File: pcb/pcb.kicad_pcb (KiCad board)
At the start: 2 copper layers, 27 parts, among them J1 Screw_Terminal_01x02, J2 Screw_Terminal_01x04, J3 Screw_Terminal_01x04, J4 Screw_Terminal_01x03, J5 Screw_Terminal_01x06, Q1 2N7000, Q2 2N7000, Q3 2N7000

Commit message: fix power line
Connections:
- A1 pad 1: Net-(A1-VMOT) -> Net-(D1-A)
- A1 pad 7: Net-(D1-K) -> Net-(D1-A)
- A2 pad 1: Net-(A1-VMOT) -> Net-(D1-A)
- A2 pad 7: unconnected-(A2-GND-Pad7) -> Net-(D1-A)
- A2 pad 8: unconnected-(A2-VMOT-Pad8) -> Net-(A1-VMOT)
- D1 pad 1: Net-(D1-K) -> Net-(A1-VMOT)
- D1 pad 2: Net-(A1-VMOT) -> Net-(D1-A)
- ESP32-S3 pad 22: Net-(A1-VMOT) -> Net-(D1-A)
- InputCap1 pad 1: Net-(A1-VMOT) -> Net-(D1-A)
- InputCap2 pad 1: Net-(A1-VMOT) -> Net-(D1-A)
- InputCap2 pad 2: Net-(D1-K) -> Net-(A1-VMOT)
- J1 pad 1: Net-(A1-VMOT) -> Net-(D1-A)
- J1 pad 2: Net-(D1-K) -> Net-(A1-VMOT)
- MovingBumperStart1 pad 1: Net-(A1-VMOT) -> Net-(D1-A)
- MovingBumper_back1 pad 1: Net-(A1-VMOT) -> Net-(D1-A)
- MovingBumper_front1 pad 1: Net-(A1-VMOT) -> Net-(D1-A)
- OutputCap1 pad 1: Net-(A1-VMOT) -> Net-(D1-A)
- OutputCap2 pad 1: Net-(A1-VMOT) -> Net-(D1-A)
- PTCFuse1 pad 1: Net-(D1-K) -> Net-(A1-VMOT)
- Q1 pad 1: Net-(A1-VMOT) -> Net-(D1-A)
- Q2 pad 1: Net-(A1-VMOT) -> Net-(D1-A)
- Q3 pad 1: Net-(A1-VMOT) -> Net-(D1-A)
- R1 pad 2: Net-(A1-VMOT) -> Net-(D1-A)
- Regulator1 pad 1: Net-(A1-VMOT) -> Net-(D1-A)
- Rehydration_bumper1 pad 1: Net-(A1-VMOT) -> Net-(D1-A)

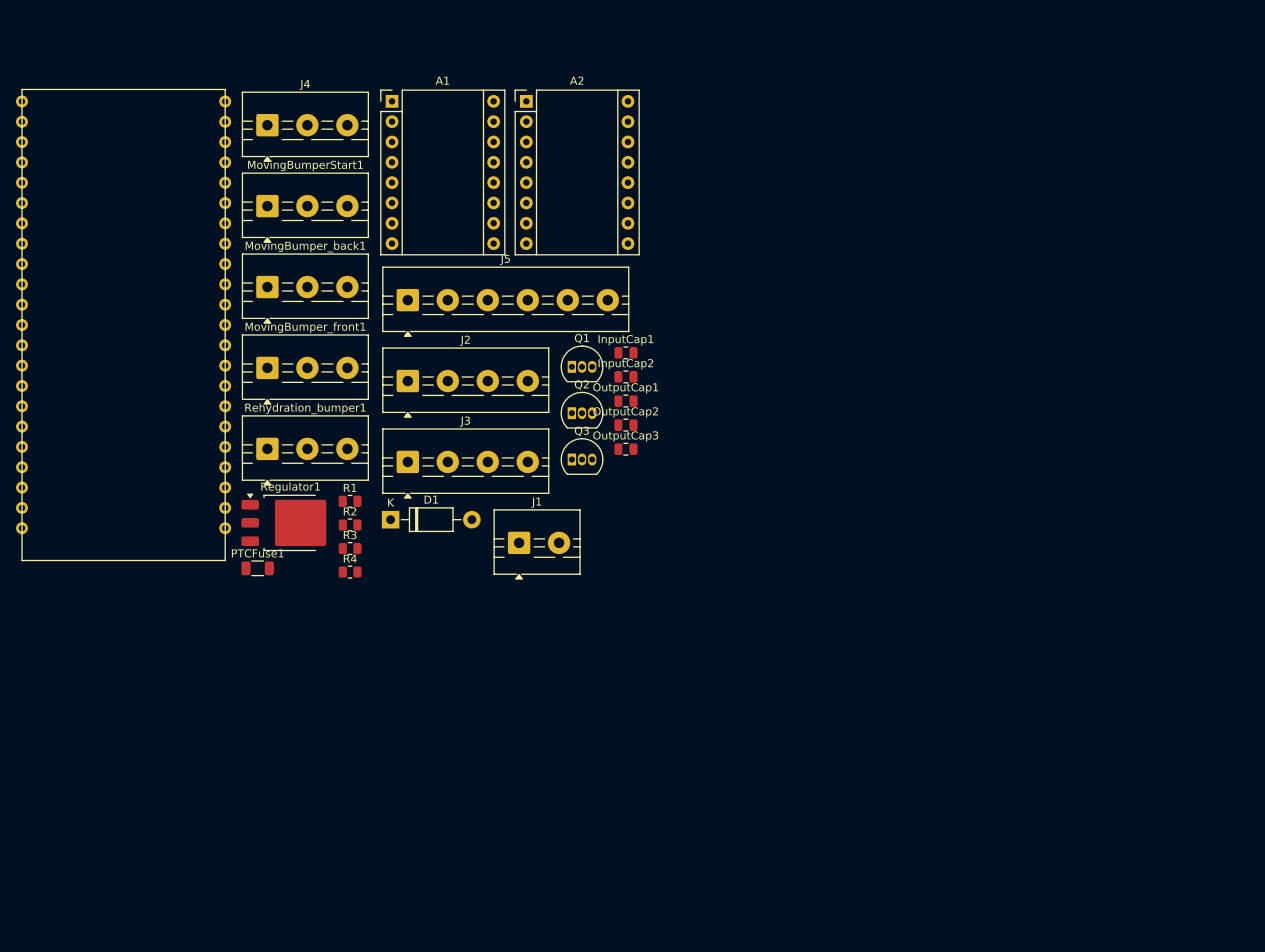
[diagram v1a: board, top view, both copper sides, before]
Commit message: auto-routed pcb, might make smaller or a better layout
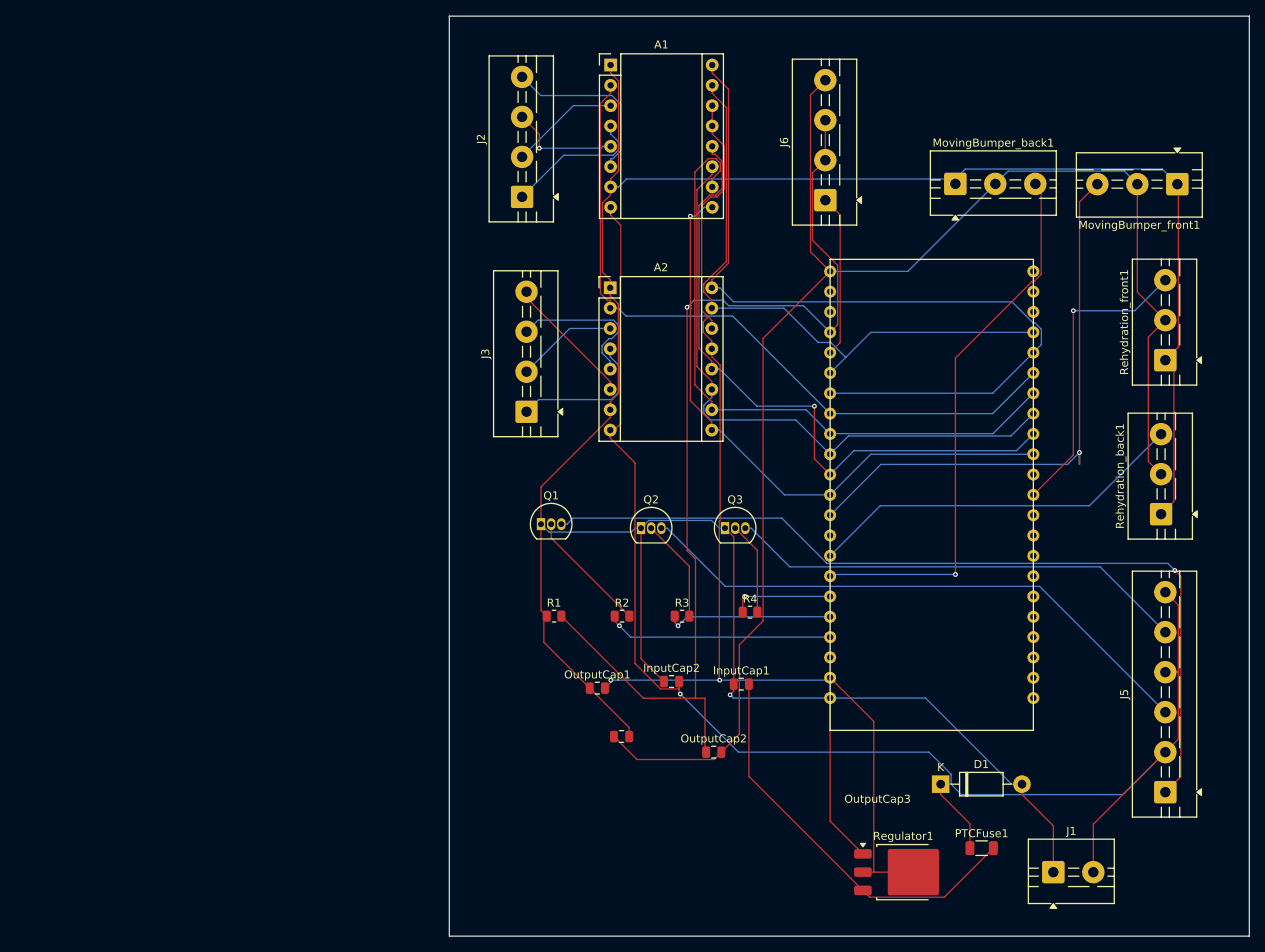
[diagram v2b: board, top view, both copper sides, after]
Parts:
- removed J4, MovingBumperStart1, Rehydration_bumper1: Screw_Terminal_01x03, TerminalBlock:TerminalBlock_MaiXu_MX126-5.0-03P_1x03_P5.00mm
- added J6: Screw_Terminal_01x04, TerminalBlock:TerminalBlock_MaiXu_MX126-5.0-04P_1x04_P5.00mm, F.Cu at (158.5, 58.0)
- added Rehydration_back1: Screw_Terminal_01x03, TerminalBlock:TerminalBlock_MaiXu_MX126-5.0-03P_1x03_P5.00mm, F.Cu at (200.5, 97.2)
- added Rehydration_front1: Screw_Terminal_01x03, TerminalBlock:TerminalBlock_MaiXu_MX126-5.0-03P_1x03_P5.00mm, F.Cu at (201.0, 78.0)
- OutputCap2: value 10uF -> 0.01uF
- OutputCap3: value 10uF -> 2.2uF
- R2, R4: value 4.6k -> 1k
- R3: value 4.6k -> 1k'
- moved MovingBumper_front1 116.0 mm to (202.5, 56.0), turned to 180 degrees
- moved J5 112.9 mm to (201.0, 132.0), turned to 90 degrees
- moved ESP32-S3 103.2 mm to (159.1, 66.9)
- moved PTCFuse1 97.0 mm to (178.0, 139.0)
- moved Regulator1 88.2 mm to (168.2, 142.0)
- moved MovingBumper_back1 87.0 mm to (174.8, 56.0)
- moved J1 78.4 mm to (187.0, 142.0)
- moved D1 76.3 mm to (172.9, 131.0)
- moved R4 50.2 mm to (149.1, 109.5)
- moved InputCap1 43.9 mm to (148.0, 118.5)
- moved R3 42.4 mm to (140.6, 110.0)
- moved OutputCap2 42.3 mm to (144.6, 127.0)
- moved InputCap2 38.5 mm to (139.3, 118.2)
- moved OutputCap1 36.1 mm to (130.0, 119.0)
- moved OutputCap3 35.9 mm to (133.0, 125.0)
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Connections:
- net Net-(ESP32-S3-10) renamed /B_B
- net Net-(ESP32-S3-11) renamed /Mix3
- net Net-(ESP32-S3-12) renamed /Mix2
- net Net-(ESP32-S3-13) renamed /Mix1
- net Net-(ESP32-S3-3) renamed /B_F
- A1 pad 10: Net-(A1-M0) -> /M0
- A1 pad 11: Net-(A1-M1) -> /M1
- A1 pad 12: Net-(A1-M2) -> /M2
- A1 pad 13: Net-(A1-~{RST}) -> /5V
- A1 pad 14: Net-(A1-~{RST}) -> /5V
- A1 pad 15: Net-(A1-STEP) -> /STEP
- A1 pad 16: Net-(A1-DIR) -> /DIR
- A1 pad 2: Net-(A1-~{FLT}) -> /FLT
- A1 pad 9: Net-(A1-~{EN}) -> /EN
- A2 pad 10: Net-(A2-M0) -> /M0
- A2 pad 11: Net-(A2-M1) -> /M1
- A2 pad 12: Net-(A2-M2) -> /M2
- A2 pad 13: Net-(A1-~{RST}) -> /5V
- A2 pad 14: Net-(A1-~{RST}) -> /5V
- A2 pad 15: Net-(A2-STEP) -> /STEP
- A2 pad 16: Net-(A2-DIR) -> /DIR
- A2 pad 2: Net-(A2-~{FLT}) -> /FLT
- A2 pad 9: Net-(A2-~{EN}) -> /EN
- ESP32-S3 pad 1: unconnected-(ESP32-S3-3V3-Pad1) -> Net-(J6-Pin_4)
- ESP32-S3 pad 10: Net-(A2-M1) -> /M1
- ESP32-S3 pad 11: Net-(A2-M2) -> /M2
- ESP32-S3 pad 12: Net-(A2-~{EN}) -> /EN
- ESP32-S3 pad 15: Net-(ESP32-S3-9) -> /R_B
- ESP32-S3 pad 21: Net-(A1-~{RST}) -> /5V
- ESP32-S3 pad 26: Net-(A1-STEP) -> /STEP
- ESP32-S3 pad 27: Net-(A1-DIR) -> /DIR
- ESP32-S3 pad 28: Net-(A1-~{FLT}) -> /FLT
- ESP32-S3 pad 29: Net-(A1-M0) -> /M0
- ESP32-S3 pad 30: Net-(A1-M1) -> /M1
- ESP32-S3 pad 31: Net-(A1-M2) -> /M2
- ESP32-S3 pad 32: Net-(A1-~{EN}) -> /EN
- ESP32-S3 pad 34: Net-(ESP32-S3-36) -> /R_F
- ESP32-S3 pad 4: Net-(J4-Pin_1) -> /VD_o
- ESP32-S3 pad 5: unconnected-(ESP32-S3-Pad5) -> /Heating_pwm
- ESP32-S3 pad 6: Net-(A2-STEP) -> /STEP
- ESP32-S3 pad 7: Net-(A2-DIR) -> /DIR
- ESP32-S3 pad 8: Net-(A2-~{FLT}) -> /FLT
- ESP32-S3 pad 9: Net-(A2-M0) -> /M0
- J5 pad 2: Net-(A1-~{RST}) -> Net-(A1-VMOT)
- J5 pad 4: Net-(A1-~{RST}) -> Net-(A1-VMOT)
- J5 pad 6: Net-(A1-~{RST}) -> Net-(A1-VMOT)
- MovingBumper_back1 pad 2: Net-(A1-~{RST}) -> Net-(J6-Pin_4)
- MovingBumper_front1 pad 2: Net-(A1-~{RST}) -> Net-(J6-Pin_4)
- OutputCap1 pad 2: Net-(A1-~{RST}) -> /5V
- OutputCap2 pad 1: Net-(D1-A) -> /VD_o
- OutputCap2 pad 2: Net-(A1-~{RST}) -> Net-(J6-Pin_4)
- OutputCap3 pad 1: Net-(J4-Pin_1) -> Net-(J6-Pin_4)
- OutputCap3 pad 2: Net-(J4-Pin_2) -> Net-(D1-A)
- R1 pad 1: Net-(J4-Pin_1) -> Net-(D1-A)
- R1 pad 2: Net-(D1-A) -> /VD_o
- Regulator1 pad 2: Net-(A1-~{RST}) -> /5V
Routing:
- net Net-(D1-A): track 0.00 -> 352.5 mm, vias 0 -> 1
- net Net-(J6-Pin_4): track 0.00 -> 189.9 mm
- net Net-(A1-VMOT): track 0.00 -> 189.6 mm, vias 0 -> 1
- net /5V: track 0.00 -> 138.9 mm, vias 0 -> 2
- net /VD_o: track 0.00 -> 127.1 mm, vias 0 -> 1
- net Net-(J5-Pin_1): track 0.00 -> 108.5 mm, vias 0 -> 1
- net /DIR: track 0.00 -> 103.7 mm
- net /FLT: track 0.00 -> 89.6 mm
- net /M2: track 0.00 -> 82.5 mm, vias 0 -> 1
- net /M0: track 0.00 -> 81.6 mm
- net /M1: track 0.00 -> 78.2 mm
- net /STEP: track 0.00 -> 77.0 mm
- net /EN: track 0.00 -> 76.8 mm, vias 0 -> 1
- net /B_F: track 0.00 -> 74.8 mm, vias 0 -> 1
- net Net-(J5-Pin_3): track 0.00 -> 72.5 mm
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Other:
- board outline added: 100 x 115 mm

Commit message: finished layout
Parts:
- added ExtraTerminalBlock1: Screw_Terminal_01x04, TerminalBlock:TerminalBlock_MaiXu_MX126-5.0-04P_1x04_P5.00mm, F.Cu at (166.2, 134.4)
- moved J5 97.1 mm to (103.9, 129.6)
- moved J1 73.0 mm to (114.2, 137.0)
- moved PTCFuse1 64.1 mm to (114.8, 128.5)
- moved J3 59.8 mm to (165.0, 125.1)
- moved vd_c2 59.3 mm to (117.6, 67.8)
- moved vd_c1 57.9 mm to (124.5, 72.7)
- moved MovingBumper_front1 55.1 mm to (147.4, 57.7)
- moved MovingBumper_back1 54.8 mm to (120.0, 57.5)
- moved A2 52.2 mm to (172.0, 102.1), turned to 180 degrees
- moved D1 51.8 mm to (121.1, 128.5)
- moved J6 49.3 mm to (109.2, 56.0), turned to -90 degrees
- moved Rehydration_back1 44.6 mm to (166.7, 68.0), turned to -90 degrees
- moved vd_r1 42.5 mm to (123.3, 67.5)
- moved A1 42.5 mm to (111.1, 78.3)
- moved Rehydration_front1 40.9 mm to (165.2, 58.0), turned to 180 degrees
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- renumbered R2 to mix1, R3 to mix2, R4 to mix3, InputCap2 to motor_c1, InputCap1 to reg_ci1, OutputCap1 to reg_co1, OutputCap2 to vd_c1, OutputCap3 to vd_c2, R1 to vd_r1
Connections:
- ESP32-S3 pad 40: unconnected-(ESP32-S3-21-Pad40) -> Net-(ESP32-S3-21)
- ESP32-S3 pad 41: unconnected-(ESP32-S3-20-Pad41) -> Net-(ESP32-S3-20)
- ESP32-S3 pad 44: unconnected-(ESP32-S3-GND-Pad44) -> Net-(ExtraTerminalBlock1-Pin_3)
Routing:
- net Net-(D1-A): track 352.5 -> 254.5 mm
- net /VD_o: track 127.1 -> 35.5 mm
- net Net-(J5-Pin_1): track 108.5 -> 20.5 mm, vias 1 -> 0
- net Net-(J5-Pin_3): track 72.5 -> 13.4 mm
- net Net-(J5-Pin_5): track 57.9 -> 12.1 mm
- net /M0: track 81.6 -> 42.0 mm
- net /DIR: track 103.7 -> 65.0 mm
- net /M1: track 78.2 -> 41.3 mm
- net /EN: track 76.8 -> 40.9 mm, vias 1 -> 0
- net /M2: track 82.5 -> 50.7 mm, vias 1 -> 0
- net /B_F: track 74.8 -> 44.2 mm, vias 1 -> 0
- net Net-(ESP32-S3-21): track 0.00 -> 28.5 mm
- net Net-(A1-VMOT): track 189.6 -> 163.6 mm
- net Net-(ESP32-S3-20): track 0.00 -> 23.9 mm
- net /5V: track 138.9 -> 117.9 mm, vias 2 -> 1
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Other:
- board size 100 x 115 mm -> 79 x 95 mm

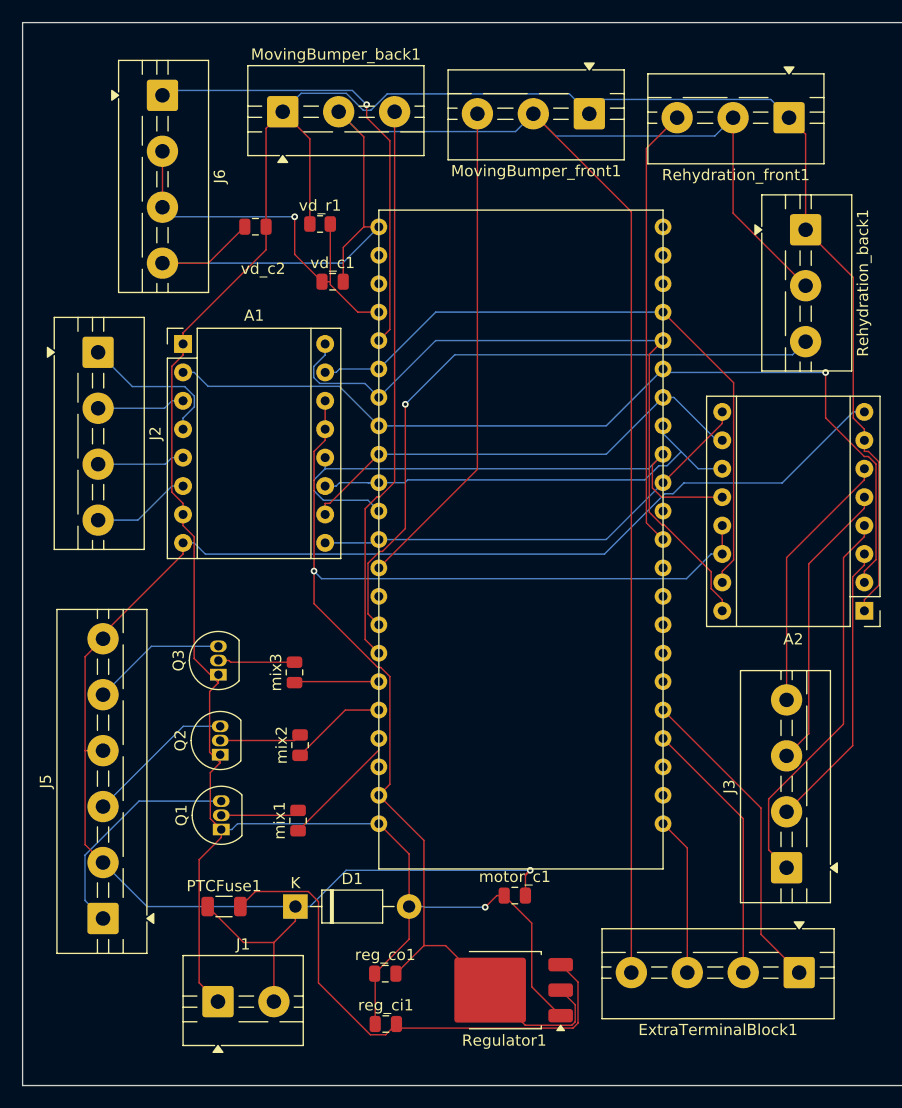
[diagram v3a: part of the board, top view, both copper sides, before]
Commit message: edit names of blocks
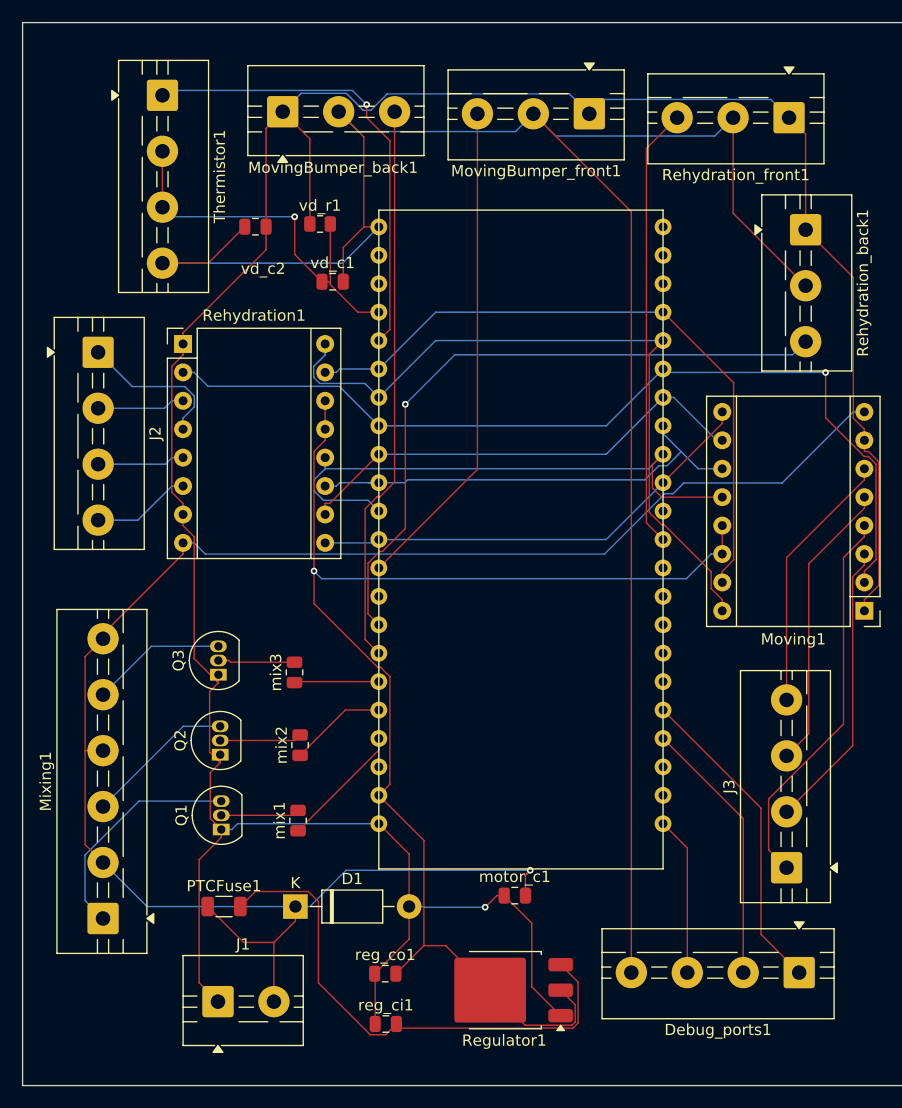
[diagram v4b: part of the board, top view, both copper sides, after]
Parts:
- renumbered ExtraTerminalBlock1 to Debug_ports1, J5 to Mixing1, A2 to Moving1, A1 to Rehydration1, J6 to Thermistor1
